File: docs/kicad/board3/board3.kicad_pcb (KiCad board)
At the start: 2 copper layers, 49.5 x 75.5 mm, 23 parts, among them J1 5V_JUMP, J2 Connector, M1 BUCK01, Q1 IRLZ44N, SW1 BUTTON1, SW2 BUTTON2, SW3 BUTTON3, U1 ESP32_DEV_0

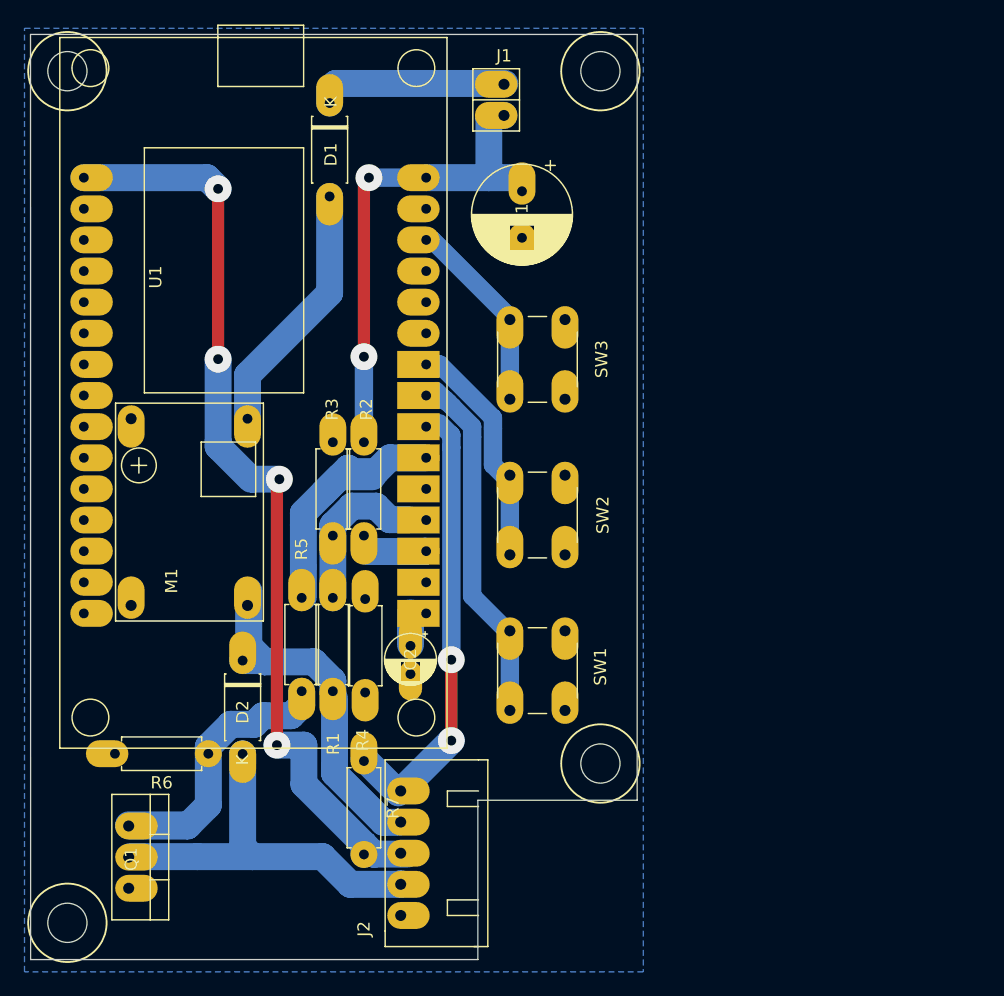
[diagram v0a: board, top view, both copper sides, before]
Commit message: Power ideaSpark board via 3.3V line instead of VIN
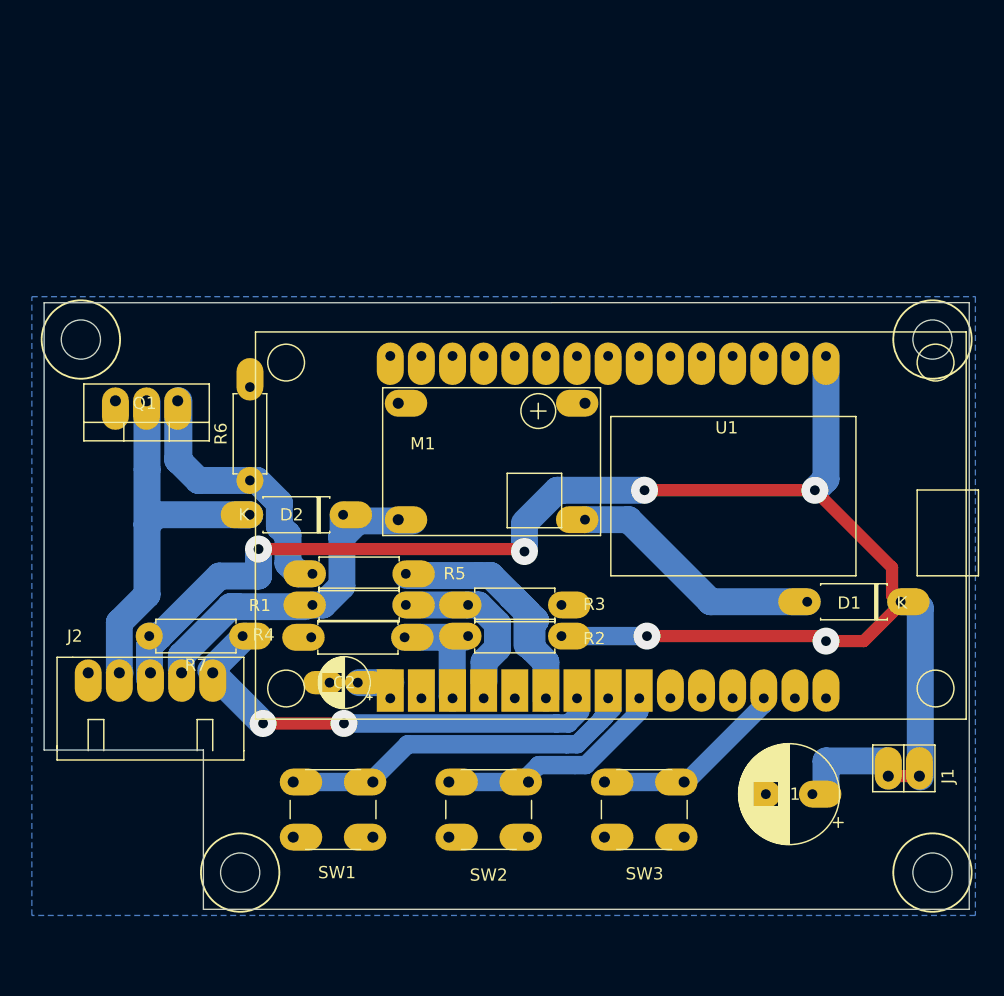
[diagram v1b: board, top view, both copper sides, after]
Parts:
- removed the REF** at (58.0, 47.5)
- removed the REF** at (101.5, 47.5)
- removed the REF** at (101.5, 104.0)
- added REF**: myMountingHole_3.2mm_M3, 0_my_footprints:myMountingHole_3.2mm_M3, F.Cu at (128.6, 69.4)
- added REF**: myMountingHole_3.2mm_M3, 0_my_footprints:myMountingHole_3.2mm_M3, F.Cu at (128.6, 112.9)
- added REF**: myMountingHole_3.2mm_M3, 0_my_footprints:myMountingHole_3.2mm_M3, F.Cu at (72.1, 112.9)
- J1: value 5V_JUMP -> USELESS_JUMP
- R2: value 10K -> 4.7K
- moved J1 65.9 mm to (127.5, 105.0), turned to 270 degrees
- moved D1 61.9 mm to (126.0, 90.8), turned to 180 degrees
- moved C1 54.6 mm to (118.8, 106.5), turned to 180 degrees
- moved REF** 47.6 mm to (59.1, 69.4), turned to 0 degrees
- moved SW3 43.3 mm to (108.3, 110.0), turned to 180 degrees
- moved Q1 34.9 mm to (67.0, 74.4), turned to 180 degrees
- moved J2 32.3 mm to (59.7, 96.6), turned to 0 degrees
- moved SW2 29.7 mm to (95.6, 110.0), turned to 180 degrees
- moved M1 27.3 mm to (85.0, 74.6), turned to 0 degrees
- moved SW1 23.0 mm to (82.9, 110.0), turned to 180 degrees
- moved R3 22.9 mm to (98.3, 91.1), turned to 180 degrees
- moved R6 22.6 mm to (72.9, 80.9), turned to 90 degrees
- moved D2 14.5 mm to (80.5, 83.7), turned to 180 degrees
- moved R7 14.2 mm to (72.3, 93.6), turned to 180 degrees
- moved R2 11.8 mm to (90.7, 93.6), turned to 0 degrees
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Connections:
- net Net-(C2-Pad1) renamed EN
- net S_5V renamed S_3V
- C1 pad 1: +5V -> +3V3
- D1 pad 1: Net-(D1-Pad1) -> +3V3
- J1 pad 1: Net-(D1-Pad1) -> +3V3
- J1 pad 2: +5V -> +3V3
- R2 pad 2: +5V -> +3V3
- U1 pad 1: +5V -> Net-(U1-Pad1)
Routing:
- net +3V3: track 78.5 -> 146.2 mm, vias 4 -> 6
- net +5V: track 40.3 -> 0.00 mm, vias 2 -> 0
- net Net-(D1-Pad1): track 15.6 -> 0.00 mm
- net S_3V: track 4.89 -> 9.77 mm
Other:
- board size 49.5 x 75.5 mm -> 75.5 x 49.5 mm
